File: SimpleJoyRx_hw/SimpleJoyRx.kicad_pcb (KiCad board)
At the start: 4 copper layers, 24 x 97 mm, 108 parts, among them Q1 IRF9358, Q2 2N7002, Q3 IRLML0030, Q4 IRLML0030, SW1 DIPx8, SW2 IT-1187A, SW3 1P2T, U1 USBLC6

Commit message: Proceeding
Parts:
- removed U1: USBLC6, SOT:SOT23-6
- SW3: value 1P2T -> SS-12F23; footprint BtnsSwitches:SW_SS-1P2T -> BtnsSwitches:SW_SS-12F23
- moved Logo3 6.02 mm to (136.0, 73.8), turned to 180 degrees
- moved XL1 4.66 mm to (146.5, 78.5)
- moved SW3 4.32 mm to (143.2, 99.2), turned to 90 degrees
- moved C26 4.17 mm to (143.5, 81.0), turned to 180 degrees
- moved R9 3.19 mm to (146.2, 99.3)
- moved R10 3.16 mm to (146.2, 96.1)
- moved SW2 3.05 mm to (142.4, 78.8)
- moved XL8 2.22 mm to (140.8, 105.4)
- moved Q2 1.61 mm to (143.6, 89.7)
- moved R7 1.61 mm to (143.6, 87.0)
- moved C35 1.20 mm to (134.3, 72.0)
- moved C40 1.20 mm to (134.3, 70.7)
- moved L2 1.20 mm to (136.0, 71.2)
- moved BLN1 1.10 mm to (136.7, 73.6)
- moved C37 1.10 mm to (140.2, 73.2)
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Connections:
- DD2 pad 3: Net-(DD2-Pad3) -> (no net)
- SW3 pad 3: Net-(SW3-Pad3) -> (no net)
- XL2 pad 2: /D_IN- -> /D-
- XL2 pad 3: /D_IN+ -> /D+
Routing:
- net /D_IN+: track 20.5 -> 0.00 mm
- net GNDPWR: track 194.2 -> 213.7 mm
- net +BATT: track 38.0 -> 25.1 mm, vias 3 -> 2
- net /A3: track 45.1 -> 35.4 mm
- net GND: track 228.7 -> 237.3 mm
- net Net-(C26-Pad1): track 8.17 -> 0.00 mm
- net /DIR1: track 31.6 -> 24.1 mm
- net /A4: track 43.4 -> 36.0 mm
- net Net-(C27-Pad1): track 6.92 -> 0.00 mm
- net /PWM3: track 27.8 -> 22.7 mm, vias 2 -> 1
- net VAA: track 39.0 -> 34.9 mm
- net +3.3V: track 110.4 -> 106.6 mm
- net /D_IN-: track 20.0 -> 16.8 mm
- net Net-(DD2-Pad17): track 3.01 -> 0.00 mm
- net /PWM4: track 28.4 -> 25.4 mm
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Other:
- net class Default: trace_width 0.25 -> 0.15; via_dia 0.7 -> 0.6
- board text added: "SimpleJoy RX 2.1"
- board text removed: "SimpleJoy RX 2.0"

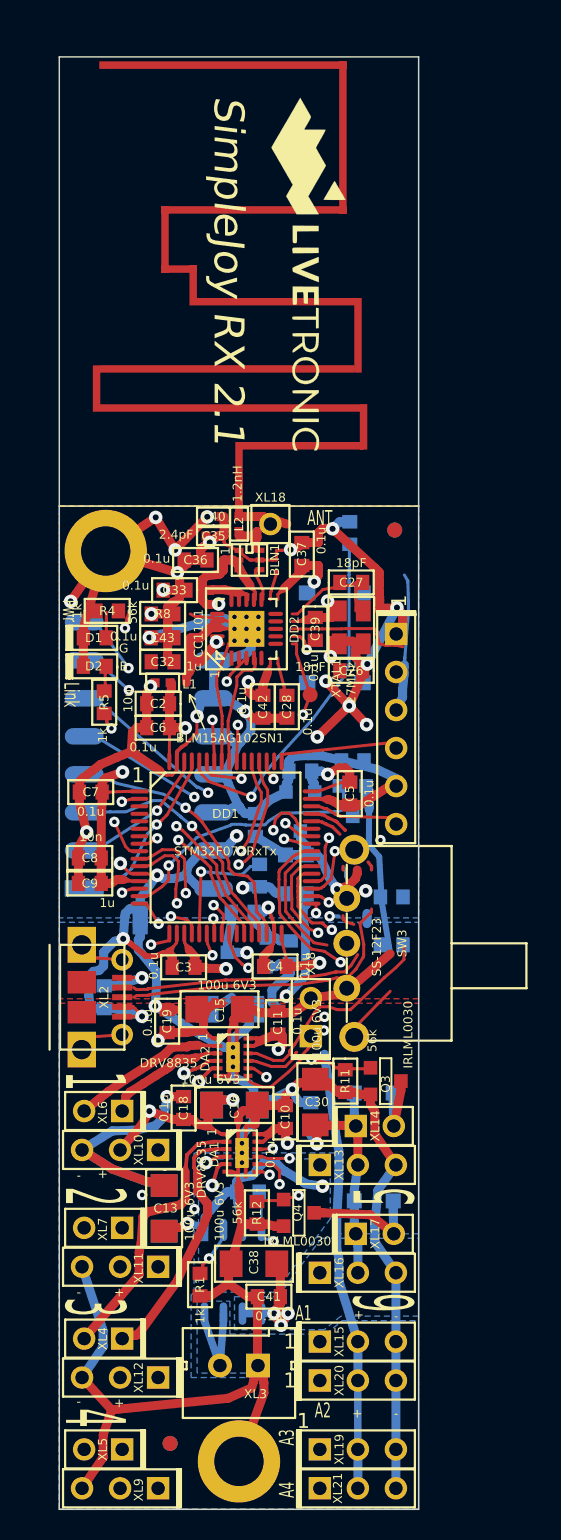
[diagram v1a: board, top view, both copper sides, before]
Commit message: * rPkt format changed * Rx v3 done Seems working
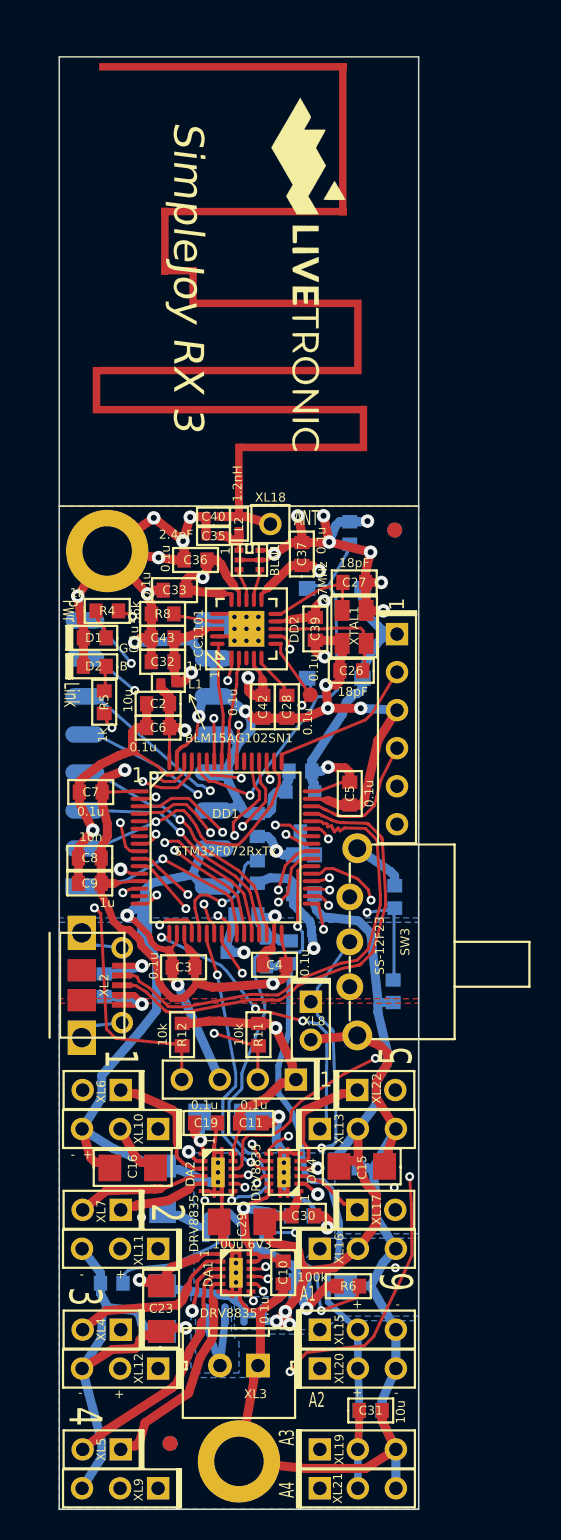
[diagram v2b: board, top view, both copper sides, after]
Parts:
- removed C38: 100u 6V3, Capacitors:CAP_1206
- removed C41: 0.1u, Capacitors:CAP_0603
- removed D5, D6: PMEG2020, Diodes:SOD323
- removed Q2: 2N7002, SOT:SOT23-3
- removed Q3, Q4: IRLML0030, SOT:SOT23-3
- removed R7: 100k, Resistors:RES_0603
- added C22: 0.1u, Capacitors:CAP_0603, B.Cu at (140.2, 117.4)
- added C23: 100u 6V3, Capacitors:CAP_1206, F.Cu at (130.8, 123.6)
- added C29: 100u 6V3, Capacitors:CAP_1206, F.Cu at (136.2, 117.8)
- added C34: 0.1u, Capacitors:CAP_0603, B.Cu at (144.8, 130.4)
- added DA4: DRV8835, QFN_DFN:WSON12, F.Cu at (139.0, 114.5)
- added XL22: PLS2, Connectors:PLS-2, F.Cu at (143.9, 109.0)
- C13, C18, R1: moved to B.Cu
- C30: value 100u 6V3 -> 0.1u; footprint Capacitors:CAP_1206 -> Capacitors:CAP_0603
- C31: value 0.1u -> 10u; moved to F.Cu
- R11, R12: value 56k -> 10k
- R6: moved to F.Cu
- XL14: value PLS2 -> CONN_4; footprint Connectors:PLS-2 -> Connectors:PLS-4
- moved C17 20.5 mm to (130.9, 123.6), turned to 90 degrees
- moved C31 20.2 mm to (144.8, 130.4), turned to 0 degrees
- moved C15 14.2 mm to (144.2, 114.1)
- moved R12 12.9 mm to (132.2, 105.3)
- moved C13 11.8 mm to (141.6, 122.1), turned to 180 degrees
- moved C18 11.6 mm to (143.2, 114.2), turned to 180 degrees
- moved C10 10.4 mm to (139.0, 121.2), turned to 90 degrees
- moved R6 9.20 mm to (143.3, 122.1)
- moved DA1 8.01 mm to (135.8, 121.2)
- moved C16 7.99 mm to (128.9, 114.2), turned to 0 degrees
- moved DA2 7.76 mm to (134.6, 114.5)
- moved C30 7.64 mm to (140.3, 117.4), turned to 180 degrees
- moved C19 7.28 mm to (133.8, 111.2), turned to 180 degrees
- moved C11 6.94 mm to (136.8, 111.2), turned to 180 degrees
- moved R11 6.58 mm to (137.3, 105.3)
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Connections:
- C31 pad 1: GNDPWR -> VAA
- C31 pad 2: PwrUnst -> GNDPWR
- DD1 pad 15: /MEASURE_EN -> (no net)
- DD1 pad 26: (no net) -> /DIP1
- DD1 pad 3: (no net) -> /DIR5
- DD1 pad 4: (no net) -> /DIR6
- DD1 pad 50: (no net) -> /DIP2
- DD1 pad 61: /DIP1 -> /SCL
- DD1 pad 62: /DIP2 -> /SDA
- R10 pad 1: Net-(Q2-Pad3) -> GNDPWR
- R11 pad 1: /PWM5 -> +3.3V
- R11 pad 2: GNDPWR -> /SCL
- R12 pad 1: /PWM6 -> +3.3V
- R12 pad 2: GNDPWR -> /SDA
- R9 pad 2: +BATT -> PwrUnst
- XL14 pad 1: PwrUnst -> +3.3V
- XL14 pad 2: /PWM_OUT5 -> /SCL
- XL17 pad 1: PwrUnst -> /MOTORE2
- XL17 pad 2: /PWM_OUT6 -> /MOTORE1
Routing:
- net /DIR5: track 0.00 -> 34.2 mm, vias 0 -> 2
- net /SCL: track 0.00 -> 32.7 mm, vias 0 -> 2
- net /DIR6: track 0.00 -> 31.1 mm, vias 0 -> 2
- net /SDA: track 0.00 -> 28.8 mm, vias 0 -> 2
- net /D-: track 2.40 -> 31.2 mm
- net /D+: track 3.21 -> 31.4 mm
- net PwrUnst: track 114.2 -> 138.3 mm, vias 8 -> 5
- net +3.3V: track 106.6 -> 129.5 mm, vias 7 -> 6
- net /ANT2: track 38.6 -> 16.8 mm
- net /PWM4: track 25.4 -> 45.1 mm, vias 2 -> 3
- net /PWM3: track 22.7 -> 40.7 mm, vias 1 -> 3
- net /MEASURE_EN: track 17.8 -> 0.00 mm, vias 1 -> 0
- net /D_IN-: track 16.8 -> 0.00 mm
- net GND: track 237.3 -> 222.5 mm, vias 29 -> 27
- net /DIR1: track 24.1 -> 36.4 mm
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- removed copper zone on B.Cu, net +BATT
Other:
- board text added: "+ SCL GND SDA"
- board text added: "I2C"
- board text added: "SimpleJoy RX 3"
- board text removed: "SimpleJoy RX 2.1"
